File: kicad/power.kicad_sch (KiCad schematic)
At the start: 100 parts, among them J1 USB_C_Receptacle_USB2.0_16P, J11 Balance, J3 XT30UPB-M, Q1 AO4407A, Q2 80N03F, Q3 80N03F, SW1 Power, U13 BQ7791501, U4 AP64500SP-13, U5 CH224A, U7 BQ25798, U8 HT7550-1, U9 XC6206P332MR

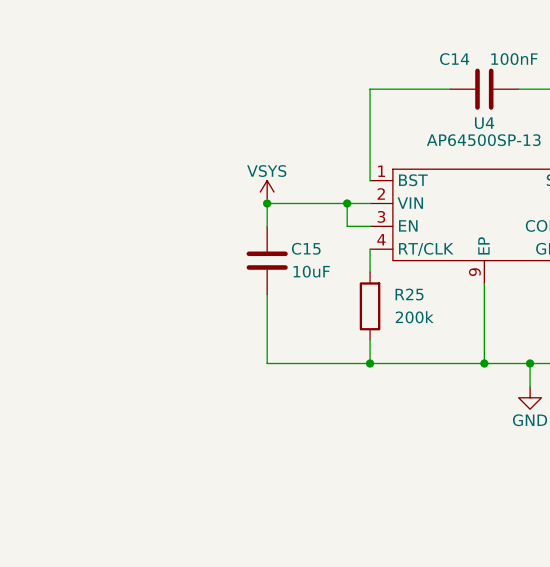
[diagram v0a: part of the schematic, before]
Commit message: Add VIN bulk caps C73/C74 and note the buck output cap height
Pulled from goosebrain 114357a: C73 (10uF 0805) and C74 (100nF 0402) on
the power sheet, and the PARTS.md note that C5/C8/C12 stay at 1206 under
the pack.

Co-Authored-By: Claude Opus 5.5 <noreply@anthropic.com>
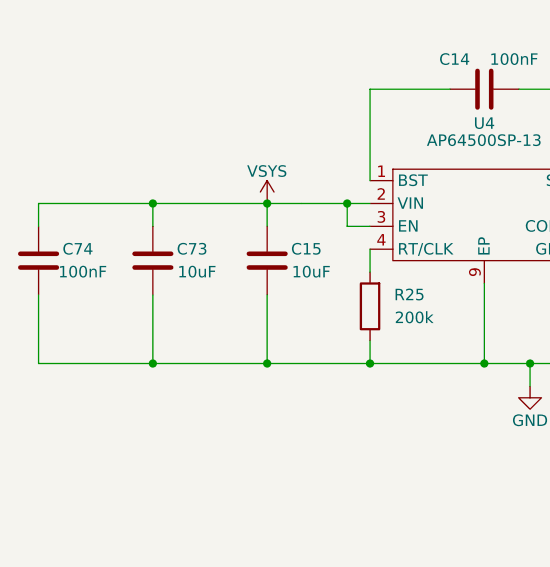
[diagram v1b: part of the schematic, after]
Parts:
- added C73: 10uF, Capacitor_SMD:C_0805_2012Metric, symbol Device:C
- added C74: 100nF, Capacitor_SMD:C_0402_1005Metric, symbol Device:C
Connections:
- net GND: now also C73.1, C74.1
- net VSYS: now also C73.2, C74.2

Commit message: Split into brain + smart pack, and support 2S packs
Brain/pack split: charging, protection and the fuse move off the brain
into a separate smart pack board (kicad-pack/goosepack), with its own
USB-C charging port. The brain drops to 4 layers, loses the charger,
PD sink, protector and SY6280, and swaps the DRV8848s for DRV8871s.

2S support on the brain:
- DRV8871 -> DRV8251A (same HSOP-8 footprint, 4.5-48 V VM). Shared VREF
  divider R107/R108/C81 from +3V3 (2.53 V) and 1.18k IPROPI resistors
  keep the 1.36 A limit.
- Q1 gate divider 27k/10k -> 47k/4.7k for -5.1 V drive at an empty 2S
  pack; C71 4.7n -> 10n to keep the ~70 us soft start.

New 2S pack variant (kicad-pack-2s/goosepack2s): BQ25798 PROG 8.2k
(2S, 750 kHz), ILIM R33 18k (~0.42 A charge), ABLIC S-8252AAH protector
in place of the BQ7791501, two HY2213-BB3A balancers with AO3400A and
47R 2512 bleed resistors, 3-pin XH balance header, R94 4.7k for trip
recovery. fab.py builds it with --board pack2s.

Several new parts still need LCSC numbers; fab.py flags each one.

Co-Authored-By: Claude Opus 5.5 <noreply@anthropic.com>
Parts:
- removed C17: 1uF, Capacitor_SMD:C_0603_1608Metric, symbol Device:C
- removed C18, C19: 47nF, Capacitor_SMD:C_0603_1608Metric, symbol Device:C
- removed C20, C21, C23, C24, C25, C27, C28, C29, C30, C31, C33, C34: 10uF, Capacitor_SMD:C_0805_2012Metric, symbol Device:C
- removed C22, C26, C32, C68: 100nF, Capacitor_SMD:C_0402_1005Metric, symbol Device:C
- removed C35: 4.7uF, Capacitor_SMD:C_0603_1608Metric, symbol Device:C
- removed C36: 1nF, Capacitor_SMD:C_0402_1005Metric, symbol Device:C
- removed C62, C63, C64, C65, C66, C67: 1uF, Capacitor_SMD:C_0402_1005Metric, symbol Device:C
- removed D1: SMBJ20A, Diode_SMD:D_SMB, symbol Device:D_TVS
- removed F1: 15A fast, Fuse:Fuse_Littelfuse-NANO2-451_453, symbol Device:Fuse
- removed J11: Balance, Connector_JST:JST_XH_B4B-XH-A_1x04_P2.50mm_Vertical, symbol Connector_Generic:Conn_01x04
- removed L2: 2.2uH, Inductor_SMD:L_Changjiang_FNR4030S, symbol Device:L
- removed LED1: green, hexy:LED_Everlight_27-21_SideView, symbol Device:LED
- removed Q2, Q3: 80N03F, Package_TO_SOT_SMD:TDSON-8-1, symbol Transistor_FET:BSC026N08NS5
- removed R29, R31, R78: 6.8k, Resistor_SMD:R_0402_1005Metric, symbol Device:R
- removed R30, R62, R63, R64, R65, R68, R69: 100, Resistor_SMD:R_0402_1005Metric, symbol Device:R
- removed R32, R76: 100k, Resistor_SMD:R_0402_1005Metric, symbol Device:R
- removed R33: 33k, Resistor_SMD:R_0402_1005Metric, symbol Device:R
- removed R34: 5.23k, Resistor_SMD:R_0402_1005Metric, symbol Device:R
- removed R35: 30.1k, Resistor_SMD:R_0402_1005Metric, symbol Device:R
- removed R36: 2.2k, Resistor_SMD:R_0402_1005Metric, symbol Device:R
- removed R37, R38, R39, R75, R77, R81: 10k, Resistor_SMD:R_0402_1005Metric, symbol Device:R
- removed R61, R72: 1k, Resistor_SMD:R_0402_1005Metric, symbol Device:R
- removed R66, R67: 5m, Resistor_SMD:R_2512_6332Metric, symbol Device:R
- removed R70: 4.7k, Resistor_SMD:R_0402_1005Metric, symbol Device:R
- removed R71, R73: 1M, Resistor_SMD:R_0402_1005Metric, symbol Device:R
- removed R74: 470k, Resistor_SMD:R_0402_1005Metric, symbol Device:R
- removed TH1: 10k B3434, Resistor_SMD:R_0603_1608Metric, symbol Device:Thermistor_NTC
- removed U13: BQ7791501, Package_SO:TSSOP-24_4.4x7.8mm_P0.65mm, symbol hexyhustle:BQ77915
- removed U5: CH224A, Package_SO:SSOP-10-1EP_3.9x4.9mm_P1mm_EP2.1x3.3mm, symbol Interface_USB:CH224K
- removed U7: BQ25798, Package_DFN_QFN:Texas_RQM0029A_VQFN-29_4x4mm_P0.4mm, symbol Battery_Management:BQ25798
- added R100, R99: 5.1k, Resistor_SMD:R_0402_1005Metric, symbol Device:R
- C71: value 4.7nF -> 10nF; LCSC Part # C1538 -> (none); MPN 0402B472K500NT -> CL05B103KB5NNNC
- D4, L1: now not fitted
- R40: value 27k -> 47k; LCSC Part # C25771 -> C25792; MPN 0402WGF2702TCE -> 0402WGF4702TCE
- R41: value 10k -> 4.7k; LCSC Part # C25744 -> C25900; MPN 0402WGF1002TCE -> 0402WGF4701TCE
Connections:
- net BAT_N is gone; now on net GND: J3.1 (Pin_1)
- net VBAT is gone; now on net PACK+: C72.1, Q1.1 (S), Q1.2 (S), Q1.3 (S), R40.1
- net GND: now also R100.2, R99.2
- net CC1: now reaches J1.A5 (CC1)
- net CC1: now also R99.1
- net CC2: now reaches J1.B5 (CC2)
- net CC2: now also R100.1
- no-connect marks 13 -> 3
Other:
- note added: "J3 takes the smart pack's XT30U-F lead (kicad-pack/goosepack): pin 1 GND = the pack's protected PACK-, pin 2 PACK+ (fused in the pack). Charging, protection and the 15 A fuse live in the pack. SW1 only drives Q1's gate; R40 holds Q1 off. Motor current flows through Q1 (AO4407A P-FET). With SW1 off nothing loads the pack, so a protector trip clears (load removal). VSYS soft start: C71 (gate-drain)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"
- note added: "PACK INPUT + POWER SWITCH"
- note added: "U8 makes 5 V from VBUS (up to 30 V in), so the MCU runs from USB alone: program it with no pack or the switch off. D2/D3 OR that with the buck's VCC. Keep U8's load to the MCU (~50 mA)."
- note added: "USB-C (PROGRAMMING)"
- note added: "USB-C: programming only (no charging). R99/R100 5.1k Rd on CC1/CC2 make it a plain 5 V sink. D+/D- continue on the MCU & USB sheet."
- note added: "Vout = 0.8 V x (1 + R26/R27) = 4.96 V EN tied to VIN: always on R25 sets the switching frequency L1: Coilcraft XAL5030-222MEC, 2.2 uH, Isat 9.2 A (30 % drop) = U4's 9.2 A max limit, so an overload ends in the buck's limit, not saturation. Hand-placed. C73/C74: VIN bulk at U4's VIN pins, beside C15."
- note removed: "3S CHARGER (BQ25798)"
- note removed: "9 V PD: R29 6.8 k on CFG1 asks a USB-PD charger for 9 V; a plain 5 V source stays at 5 V (charging is slower). CH224A pin 1 is VHV (32 V): VBUS goes straight in, C17 decouples it. CFG2/CFG3, DP/DM and PG are unused (D+/D- belong to the MCU). D1 SMBJ20A clamps VBUS. D+/D- continue on the MCU & USB sheet."
- note removed: "BATTERY + POWER SWITCH"
- note removed: "BQ7791501 standalone 3S (datasheet Fig. 9-11): OV 4.25 V, UV 2.8 V; 2.5 mOhm shunt (R66||R67) -> OCD1 14 A, OCD2 24 A, SCD 48 A, OCC 8 A. CCFG, CTRC, CTRD, CBI to VSS (3 cells, no stack, balancing on); PRES high through R75 (no HIBERNATE); R76 100k = EEPROM OCD delays. Ground: the pack's negative (BAT_N, J3 pin 1) -> shunt -> Q2 (DSG) -> Q3 (CHG) -> board GND (PACK-). Everything else runs on boar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"
- note removed: "CHARGE SAFETY WITHOUT FIRMWARE PROG: R31 + R78 (2 x 6.8 k = 13.6 k) select 3S (12.6 V) at 750 kHz. ILIM_HIZ: R32/R33 (100 k / 33 k from REGN) set 1.24 V, an input limit of about 0.30 A. Charge current stays near 0.2 A (about 0.45C of the 450 mAh pack) from 9 V (less from 5 V), even though the power-on charge-current default is 1 A. TS: R34/R35 with a fixed 10 k (R81, no pack NTC) hold TS at the 2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"
- note removed: "CHARGER CAPS"
- note removed: "I2C / INT PULL-UPS"
- note removed: "MOTORS BYPASS THE CHARGER SYS VSYS (motors, 5 V buck) comes from the pack through F1 and Q1, not from CHG_SYS: the BQ25798 BATFET is rated 6 A continuous, below the motor peaks. CHG_SYS only carries its own caps. Charging works with the power switch off. LED1 (green, side view on the top edge, seen through a small hole in the wall) is lit while charging, no firmware needed."
- note removed: "PACK PROTECTION (Ovonic 80C 3S 450 mAh, no protection board in the pack)"
- note removed: "SW1 only drives Q1's gate; R40 holds Q1 off. Motor current flows through Q1 (AO4407A P-FET). F1: 15 A very fast-acting (0453015) at the pack. The charger connects at VBAT, ahead of SW1."
- note removed: "U8 makes 5 V from VBUS (up to 30 V in), so the MCU runs from USB alone: program it with a flat pack or the switch off. D2/D3 OR that with the buck's VCC. Keep U8's load to the MCU (~50 mA)."
- note removed: "USB-C INPUT + PD SINK (CH224A)"
- note removed: "VSYS SOFT START + CLAMP C71 (gate-drain) + R41 ramp VSYS in ~70 us (3-4 A inrush). C72 (gate-source) keeps fast VBAT edges from turning Q1 on. D4 (SMF14A) clamps VSYS: ~19 V at 3 A (DRV8848 20 V max)."
- note removed: "Vout = 0.8 V x (1 + R26/R27) = 4.96 V EN tied to VIN: always on R25 sets the switching frequency L1: Isat 9.2 A (U4 limit 9.2 A max)"

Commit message: Fill in LCSC numbers, swap to stocked parts, tidy the new schematic parts
- LCSC numbers from JLC's 2026-10-19 in-stock catalog for every new part
  except the DRV8251A, which JLC doesn't stock (Global Sourcing or consign).
- 2S protector S-8252AAH -> HY2120-LB (C168778): pin-for-pin the same,
  OV 4.25 V / UV 2.80 V, stocked at JLC. R94 trip recovery still holds.
- IPROPI R101-R106 1.18k (2,341 in stock) -> 1.2k preferred (C25862),
  so the motor limit is 1.34 A.
- Fix the 2S pack board's footprint-symbol links (paths were dropped in
  the previous commit); both boards now link every footprint correctly.
- Move the VREF divider and the balancer block into clear space and
  rewrite the stale DRV8871/BQ7791501 notes on the motor and 2S sheets.

Co-Authored-By: Claude Opus 5.5 <noreply@anthropic.com>
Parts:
- C71: LCSC Part # (none) -> C15195; Manufacturer FH (Guangdong Fenghua) -> Samsung Electro-Mechanics
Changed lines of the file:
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@@
 			)
 		)
-		(property "Manufacturer" "FH (Guangdong Fenghua)"
+		(property "Manufacturer" "Samsung Electro-Mechanics"
 			(at 220.98 173.99 0)
 			(hide yes)
@@
 			)
 		)
-		(property "LCSC Part #" ""
+		(property "LCSC Part #" "C15195"
 			(at 220.98 173.99 0)
 			(hide yes)

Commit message: Swap J3 to a horizontal XT30 and compact the brain to 78 x 46.5 mm
- J3: XT30PW-M30.G.Y (C431092) on Connector_AMASS:AMASS_XT30PW-M
  horizontal, bottom edge, mouth out through the wall. Pin 1 PACK-/GND,
  pin 2 PACK+. Hole pattern checked against the Amass drawing.
- Placement compacted from 88.5 x 47 mm to 78 x 46.5 mm (-532.5 mm2,
  -12.8 %; 10.5 mm shorter). Blocks moved as units; edge connectors stay
  on their walls; buck loop and driver-beside-connector kept.
- R107/R108/C81 placed; Edge.Cuts redrawn with 2 mm corners; mounting
  holes, fiducials, GND pours and USB rule areas moved to match.
- Stale pack-envelope and vertical-XT30 fab notes removed or rewritten.
- README/PARTS: new size, placement summary, box = outline + 5 mm.

DRC: no clearance or courtyard errors, no parts outside the outline.

Co-Authored-By: Claude Opus 5.5 <noreply@anthropic.com>
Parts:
- J3: value XT30UPB-M -> XT30PW-M; footprint hexy:AMASS_XT30UPB-M_1x02_P5.0mm_Vertical_EasyEDA3D -> Connector_AMASS:AMASS_XT30PW-M_1x02_P2.50mm_Horizontal; LCSC Part # C428721 -> C431092; MPN XT30UPB-M -> XT30PW-M30.G.Y
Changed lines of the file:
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@@
 			)
 		)
-		(property "Value" "XT30UPB-M"
+		(property "Value" "XT30PW-M"
 			(at 154.94 167.01 0)
 			(show_name no)
@@
 			)
 		)
-		(property "Footprint" "hexy:AMASS_XT30UPB-M_1x02_P5.0mm_Vertical_EasyEDA3D"
+		(property "Footprint" "Connector_AMASS:AMASS_XT30PW-M_1x02_P2.50mm_Horizontal"
 			(at 154.94 170.18 0)
 			(hide yes)
@@
 			)
 		)
-		(property "Description" "Generic connector, single row, 01x02, script generated (kicad-library-utils/schlib/autogen/connector/)"
+		(property "Description" "Amass XT30 male, horizontal (right-angle) THT, 15 A. Pin 1 PACK- (GND), pin 2 PACK+; mouth out through the bottom wall"
 			(at 154.94 170.18 0)
 			(hide yes)
@@
 			)
 		)
-		(property "MPN" "XT30UPB-M"
+		(property "MPN" "XT30PW-M30.G.Y"
 			(at 154.94 170.18 0)
 			(effects
@@
 			)
 		)
-		(property "LCSC Part #" "C428721"
+		(property "LCSC Part #" "C431092"
 			(at 154.94 172.72 0)
 			(hide yes)

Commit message: Place the brain double-sided at 66.3 x 34 mm, unrouted
- tools/place_double.py rebuilds the placement from scratch: parts on both
  sides, M1-M6 swapped to JST PH S2B-PH-K (C173752), J3 under J4, the
  switches in the bottom-right corner, the USB-C ESD and series resistors
  on the front between J1 and U10.
- Pulls in the 2026-10-20 schematic change (IO5/IO6 off the ADC pins,
  R109/R114 15k USB-A pull-downs).
- Reassigns U10 GPIOs for the new layout, keeping each motor on its own
  PWM slice and IO4-IO6 on slices 1 and 4; USB-A moves to GPIO26/27.
- Adds back-side fiducials FID4-FID6.
- The old partial autoroute is kept in kicad/reference/.

Co-Authored-By: Claude Opus 5.5 <noreply@anthropic.com>
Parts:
- added FID4, FID5, FID6: Fiducial, Fiducial:Fiducial_1mm_Mask2mm, symbol Mechanical:Fiducial
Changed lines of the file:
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@@
+	)
+	(symbol
+		(lib_id "Mechanical:Fiducial")
+		(at 350.52 240.03 0)
+		(unit 1)
+		(body_style 1)
+		(exclude_from_sim no)
+		(in_bom yes)
+		(on_board yes)
+		(in_pos_files yes)
+		(dnp no)
+		(property "Reference" "FID4"
+			(at 350.52 237.49 0)
+			(show_name no)
+			(do_not_autoplace no)
+			(effects
+				(font
+					(size 1.27 1.27)
+				)
+			)
+		)
+		(property "Value" "Fiducial"
+			(at 350.52 242.57 0)
+			(show_name no)
+			(do_not_autoplace no)
+			(effects
+				(font
+					(size 1.27 1.27)
+				)
+			)
+		)
+		(property "Footprint" "Fiducial:Fiducial_1mm_Mask2mm"
+			(at 350.52 240.03 0)
+			(hide yes)
+			(show_name no)
+			(do_not_autoplace no)
+			(effects
+				(font
+					(size 1.27 1.27)
+				)
+			)
+		)
+		(property "Datasheet" ""
+			(at 350.52 240.03 0)
+			(hide yes)
+			(show_name no)
+			(do_not_autoplace no)
+			(effects
+				(font
+					(size 1.27 1.27)
+				)
+			)
+		)
+		(property "Description" "Fiducial Marker"
+			(at 350.52 240.03 0)
+			(hide yes)
+			(show_name no)
+			(do_not_autoplace no)
+			(effects
+				(font
+					(size 1.27 1.27)
+				)
+			)
+		)
+		(instances
+			(project "thegoose"
+				(path "/72b1d502-e600-4337-8ef9-b222b53a12da/0021e6ae-34c0-486e-ac47-c8566b803df5"
+					(reference "FID4")
+					(unit 1)
+				)
+			)
+		)
+	)
+	(symbol
+		(lib_id "Mechanical:Fiducial")
+		(at 359.41 240.03 0)
+		(unit 1)
+		(body_style 1)
+		(exclude_from_sim no)
+		(in_bom yes)
+		(on_board yes)
+		(in_pos_files yes)
+		(dnp no)
+		(property "Reference" "FID5"
+			(at 359.41 237.49 0)
+			(show_name no)
+			(do_not_autoplace no)
+			(effects
+				(font
+					(size 1.27 1.27)
+				)
+			)
+		)
+		(property "Value" "Fiducial"
+			(at 359.41 242.57 0)
+			(show_name no)
+			(do_not_autoplace no)
+			(effects
+				(font
+					(size 1.27 1.27)
+				)
+			)
+		)
+		(property "Footprint" "Fiducial:Fiducial_1mm_Mask2mm"
+			(at 359.41 240.03 0)
+			(hide yes)
+			(show_name no)
+			(do_not_autoplace no)
+			(effects
+				(font
+					(size 1.27 1.27)
+				)
+			)
+		)
+		(property "Datasheet" ""
+			(at 359.41 240.03 0)
+			(hide yes)
+			(show_name no)
+			(do_not_autoplace no)
+			(effects
+				(font
+					(size 1.27 1.27)
+				)
+			)
+		)
+		(property "Description" "Fiducial Marker"
+			(at 359.41 240.03 0)
+			(hide yes)
+			(show_name no)
+			(do_not_autoplace no)
+			(effects
+				(font
+					(size 1.27 1.27)
+				)
+			)
+		)
+		(instances
+			(project "thegoose"
+				(path "/72b1d502-e600-4337-8ef9-b222b53a12da/0021e6ae-34c0-486e-ac47-c8566b803df5"
+					(reference "FID5")
+					(unit 1)
+				)
+			)
+		)
+	)
+	(symbol
+		(lib_id "Mechanical:Fiducial")
+		(at 369.57 240.03 0)
+		(unit 1)
+		(body_style 1)
+		(exclude_from_sim no)
+		(in_bom yes)
+		(on_board yes)
+		(in_pos_files yes)
+		(dnp no)
+		(property "Reference" "FID6"
+			(at 369.57 237.49 0)
+			(show_name no)
+			(do_not_autoplace no)
+			(effects
+				(font
+					(size 1.27 1.27)
+				)
+			)
+		)
+		(property "Value" "Fiducial"
+			(at 369.57 242.57 0)
+			(show_name no)
+			(do_not_autoplace no)
+			(effects
+				(font
+					(size 1.27 1.27)
+				)
+			)
+		)
+		(property "Footprint" "Fiducial:Fiducial_1mm_Mask2mm"
+			(at 369.57 240.03 0)
+			(hide yes)
+			(show_name no)
+			(do_not_autoplace no)
+			(effects
+				(font
+					(size 1.27 1.27)
+				)
+			)
+		)
+		(property "Datasheet" ""
+			(at 369.57 240.03 0)
+			(hide yes)
+			(show_name no)
+			(do_not_autoplace no)
+			(effects
+				(font
+					(size 1.27 1.27)
+				)
+			)
+		)
+		(property "Description" "Fiducial Marker"
+			(at 369.57 240.03 0)
+			(hide yes)
+			(show_name no)
+			(do_not_autoplace no)
+			(effects
+				(font
+					(size 1.27 1.27)
+				)
+			)
+		)
+		(instances
+			(project "thegoose"
+				(path "/72b1d502-e600-4337-8ef9-b222b53a12da/0021e6ae-34c0-486e-ac47-c8566b803df5"
+					(reference "FID6")
+					(unit 1)
+				)
+			)
+		)
 	)
 	(symbol
